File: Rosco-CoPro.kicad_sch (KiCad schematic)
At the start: 16 parts, among them IC1 MC68882FN40A, IC2 ATF22V10, J1 Conn_01x03, X1 CXO_DIP8_40M

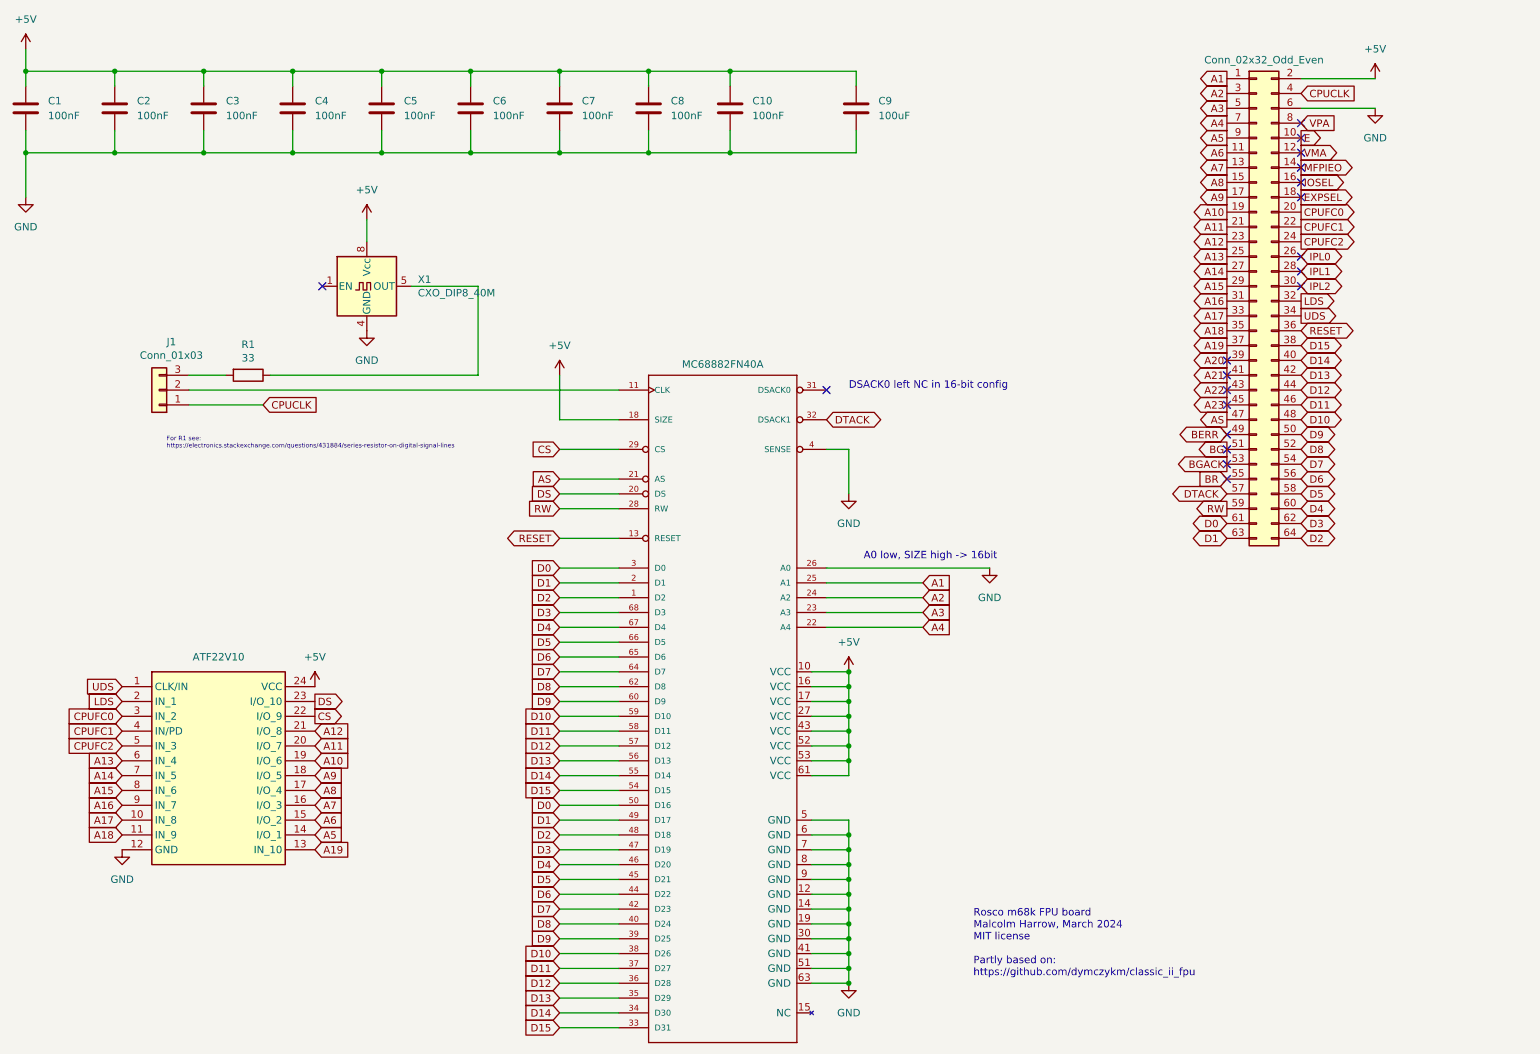
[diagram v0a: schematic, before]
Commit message: v2 board plus improvements to test suite
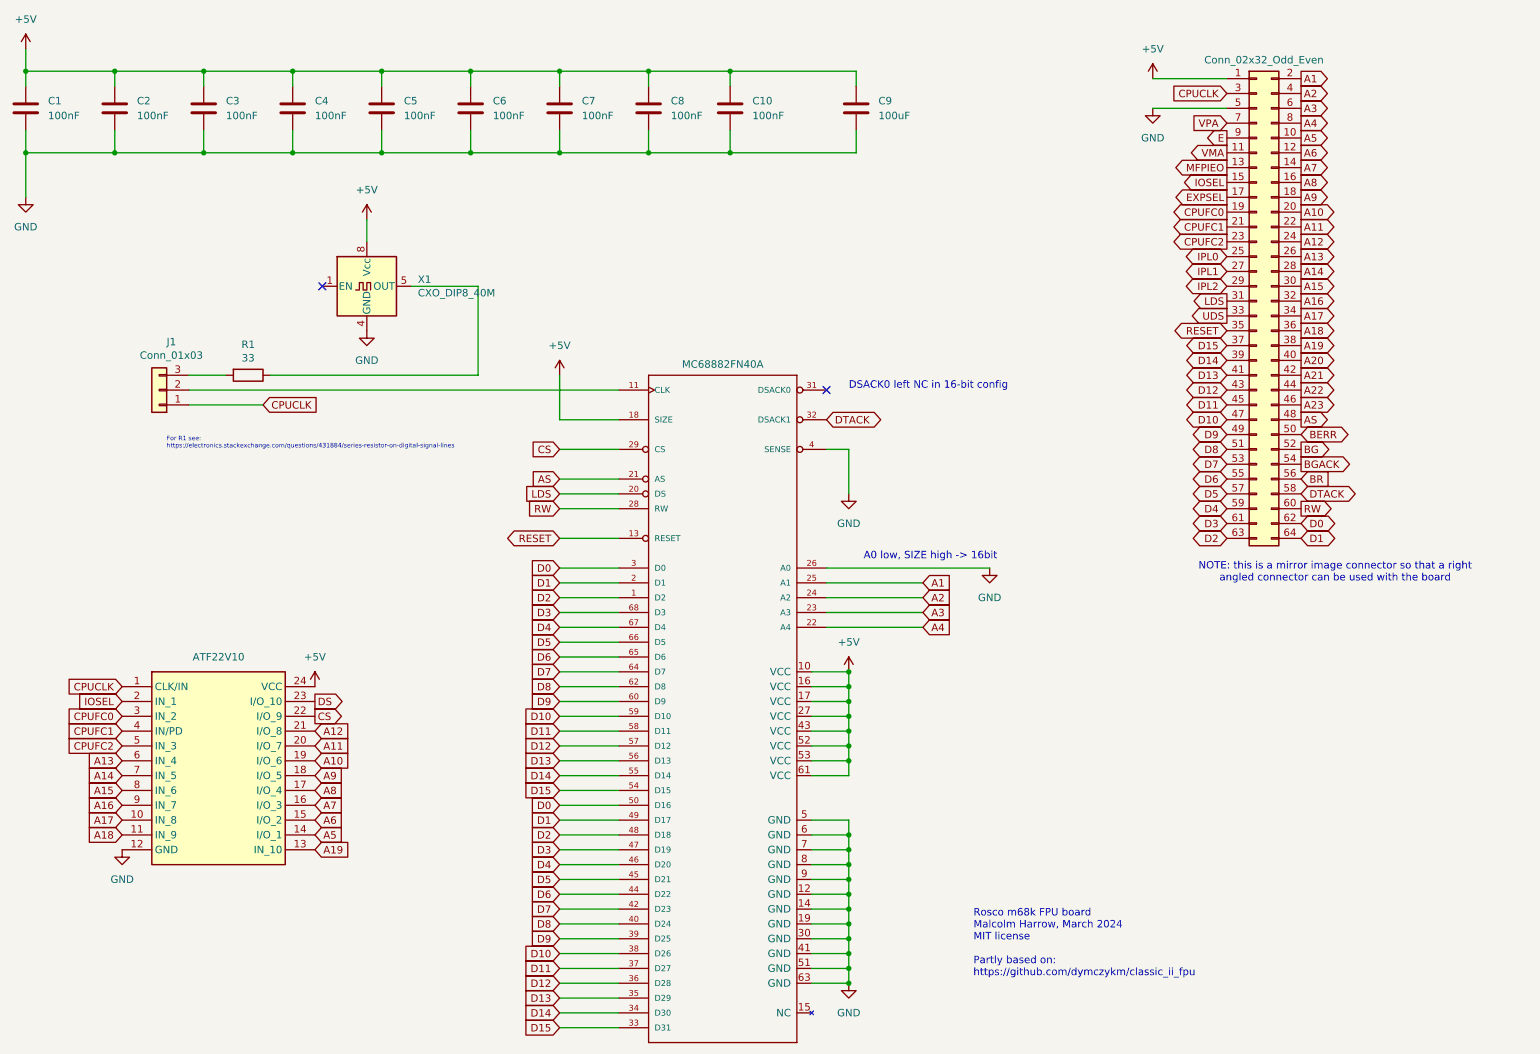
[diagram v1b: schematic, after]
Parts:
- C1, C10, C2, C3, C4, C5, C6, C7, C8: footprint Capacitor_THT:C_Disc_D3.0mm_W2.0mm_P2.50mm -> Capacitor_SMD:C_0805_2012Metric_Pad1.18x1.45mm_HandSolder; JCL (none) -> 0805; LCSC (none) -> C49678
- R1: footprint Resistor_THT:R_Axial_DIN0207_L6.3mm_D2.5mm_P10.16mm_Horizontal -> Resistor_SMD:R_0805_2012Metric_Pad1.20x1.40mm_HandSolder; JCL (none) -> 0805; LCSC (none) -> C17634
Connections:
- net +5V: now also BUS1.1 (Pin_1); no longer BUS1.2 (Pin_2)
- net A1: now also BUS1.2 (Pin_2); no longer BUS1.1 (Pin_1)
- net A10: now also BUS1.20 (Pin_20); no longer BUS1.19 (Pin_19)
- net A11: now also BUS1.22 (Pin_22); no longer BUS1.21 (Pin_21)
- net A12: now also BUS1.24 (Pin_24); no longer BUS1.23 (Pin_23)
- net A13: now also BUS1.26 (Pin_26); no longer BUS1.25 (Pin_25)
- net A14: now also BUS1.28 (Pin_28); no longer BUS1.27 (Pin_27)
- net A15: now also BUS1.30 (Pin_30); no longer BUS1.29 (Pin_29)
- net A16: now also BUS1.32 (Pin_32); no longer BUS1.31 (Pin_31)
- net A17: now also BUS1.34 (Pin_34); no longer BUS1.33 (Pin_33)
- net A18: now also BUS1.36 (Pin_36); no longer BUS1.35 (Pin_35)
- net A19: now also BUS1.38 (Pin_38); no longer BUS1.37 (Pin_37)
- net A2: now also BUS1.4 (Pin_4); no longer BUS1.3 (Pin_3)
- net A20: now also BUS1.40 (Pin_40); no longer BUS1.39 (Pin_39)
- net A21: now also BUS1.42 (Pin_42); no longer BUS1.41 (Pin_41)
- net A22: now also BUS1.44 (Pin_44); no longer BUS1.43 (Pin_43)
- net A23: now also BUS1.46 (Pin_46); no longer BUS1.45 (Pin_45)
- net A3: now also BUS1.6 (Pin_6); no longer BUS1.5 (Pin_5)
- net A4: now also BUS1.8 (Pin_8); no longer BUS1.7 (Pin_7)
- net A5: now also BUS1.10 (Pin_10); no longer BUS1.9 (Pin_9)
- net A6: now also BUS1.12 (Pin_12); no longer BUS1.11 (Pin_11)
- net A7: now also BUS1.14 (Pin_14); no longer BUS1.13 (Pin_13)
- net A8: now also BUS1.16 (Pin_16); no longer BUS1.15 (Pin_15)
- net A9: now also BUS1.18 (Pin_18); no longer BUS1.17 (Pin_17)
- net AS: now also BUS1.48 (Pin_48); no longer BUS1.47 (Pin_47)
- net BERR: now also BUS1.50 (Pin_50); no longer BUS1.49 (Pin_49)
- net BG: now also BUS1.52 (Pin_52); no longer BUS1.51 (Pin_51)
- net BGACK: now also BUS1.54 (Pin_54); no longer BUS1.53 (Pin_53)
- net BR: now also BUS1.56 (Pin_56); no longer BUS1.55 (Pin_55)
- net CPUCLK: now also BUS1.3 (Pin_3), IC2.1 (CLK/IN); no longer BUS1.4 (Pin_4)
- net CPUFC0: now also BUS1.19 (Pin_19); no longer BUS1.20 (Pin_20)
- net CPUFC1: now also BUS1.21 (Pin_21); no longer BUS1.22 (Pin_22)
- net CPUFC2: now also BUS1.23 (Pin_23); no longer BUS1.24 (Pin_24)
- net D0: now also BUS1.62 (Pin_62); no longer BUS1.61 (Pin_61)
- net D1: now also BUS1.64 (Pin_64); no longer BUS1.63 (Pin_63)
- net D10: now also BUS1.47 (Pin_47); no longer BUS1.48 (Pin_48)
- net D11: now also BUS1.45 (Pin_45); no longer BUS1.46 (Pin_46)
- net D12: now also BUS1.43 (Pin_43); no longer BUS1.44 (Pin_44)
- net D13: now also BUS1.41 (Pin_41); no longer BUS1.42 (Pin_42)
- net D14: now also BUS1.39 (Pin_39); no longer BUS1.40 (Pin_40)
- net D15: now also BUS1.37 (Pin_37); no longer BUS1.38 (Pin_38)
- net D2: now also BUS1.63 (Pin_63); no longer BUS1.64 (Pin_64)
- net D3: now also BUS1.61 (Pin_61); no longer BUS1.62 (Pin_62)
- net D4: now also BUS1.59 (Pin_59); no longer BUS1.60 (Pin_60)
- net D5: now also BUS1.57 (Pin_57); no longer BUS1.58 (Pin_58)
- net D6: now also BUS1.55 (Pin_55); no longer BUS1.56 (Pin_56)
- net D7: now also BUS1.53 (Pin_53); no longer BUS1.54 (Pin_54)
- net D8: now also BUS1.51 (Pin_51); no longer BUS1.52 (Pin_52)
- net D9: now also BUS1.49 (Pin_49); no longer BUS1.50 (Pin_50)
- net DS: no longer IC1.20 (DS)
- net DTACK: now also BUS1.58 (Pin_58); no longer BUS1.57 (Pin_57)
- net E: now also BUS1.9 (Pin_9); no longer BUS1.10 (Pin_10)
- net EXPSEL: now also BUS1.17 (Pin_17); no longer BUS1.18 (Pin_18)
- net GND: now also BUS1.5 (Pin_5); no longer BUS1.6 (Pin_6)
- net IOSEL: now also BUS1.15 (Pin_15), IC2.2 (IN_1); no longer BUS1.16 (Pin_16)
- net IPL0: now also BUS1.25 (Pin_25); no longer BUS1.26 (Pin_26)
- net IPL1: now also BUS1.27 (Pin_27); no longer BUS1.28 (Pin_28)
- net IPL2: now also BUS1.29 (Pin_29); no longer BUS1.30 (Pin_30)
- net LDS: now also BUS1.31 (Pin_31), IC1.20 (DS); no longer BUS1.32 (Pin_32), IC2.2 (IN_1)
- net MFPIEO: now also BUS1.13 (Pin_13); no longer BUS1.14 (Pin_14)
- net RESET: now also BUS1.35 (Pin_35); no longer BUS1.36 (Pin_36)
- net RW: now also BUS1.60 (Pin_60); no longer BUS1.59 (Pin_59)
- net UDS: now also BUS1.33 (Pin_33); no longer BUS1.34 (Pin_34), IC2.1 (CLK/IN)
- net VMA: now also BUS1.11 (Pin_11); no longer BUS1.12 (Pin_12)
- net VPA: now also BUS1.7 (Pin_7); no longer BUS1.8 (Pin_8)
- no-connect marks 19 -> 2
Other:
- note added: "NOTE: this is a mirror image connector so that a right angled connector can be used with the board"
